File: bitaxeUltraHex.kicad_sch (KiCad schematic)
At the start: 12 parts, among them J1 Conn_01x01, J2 Conn_01x01

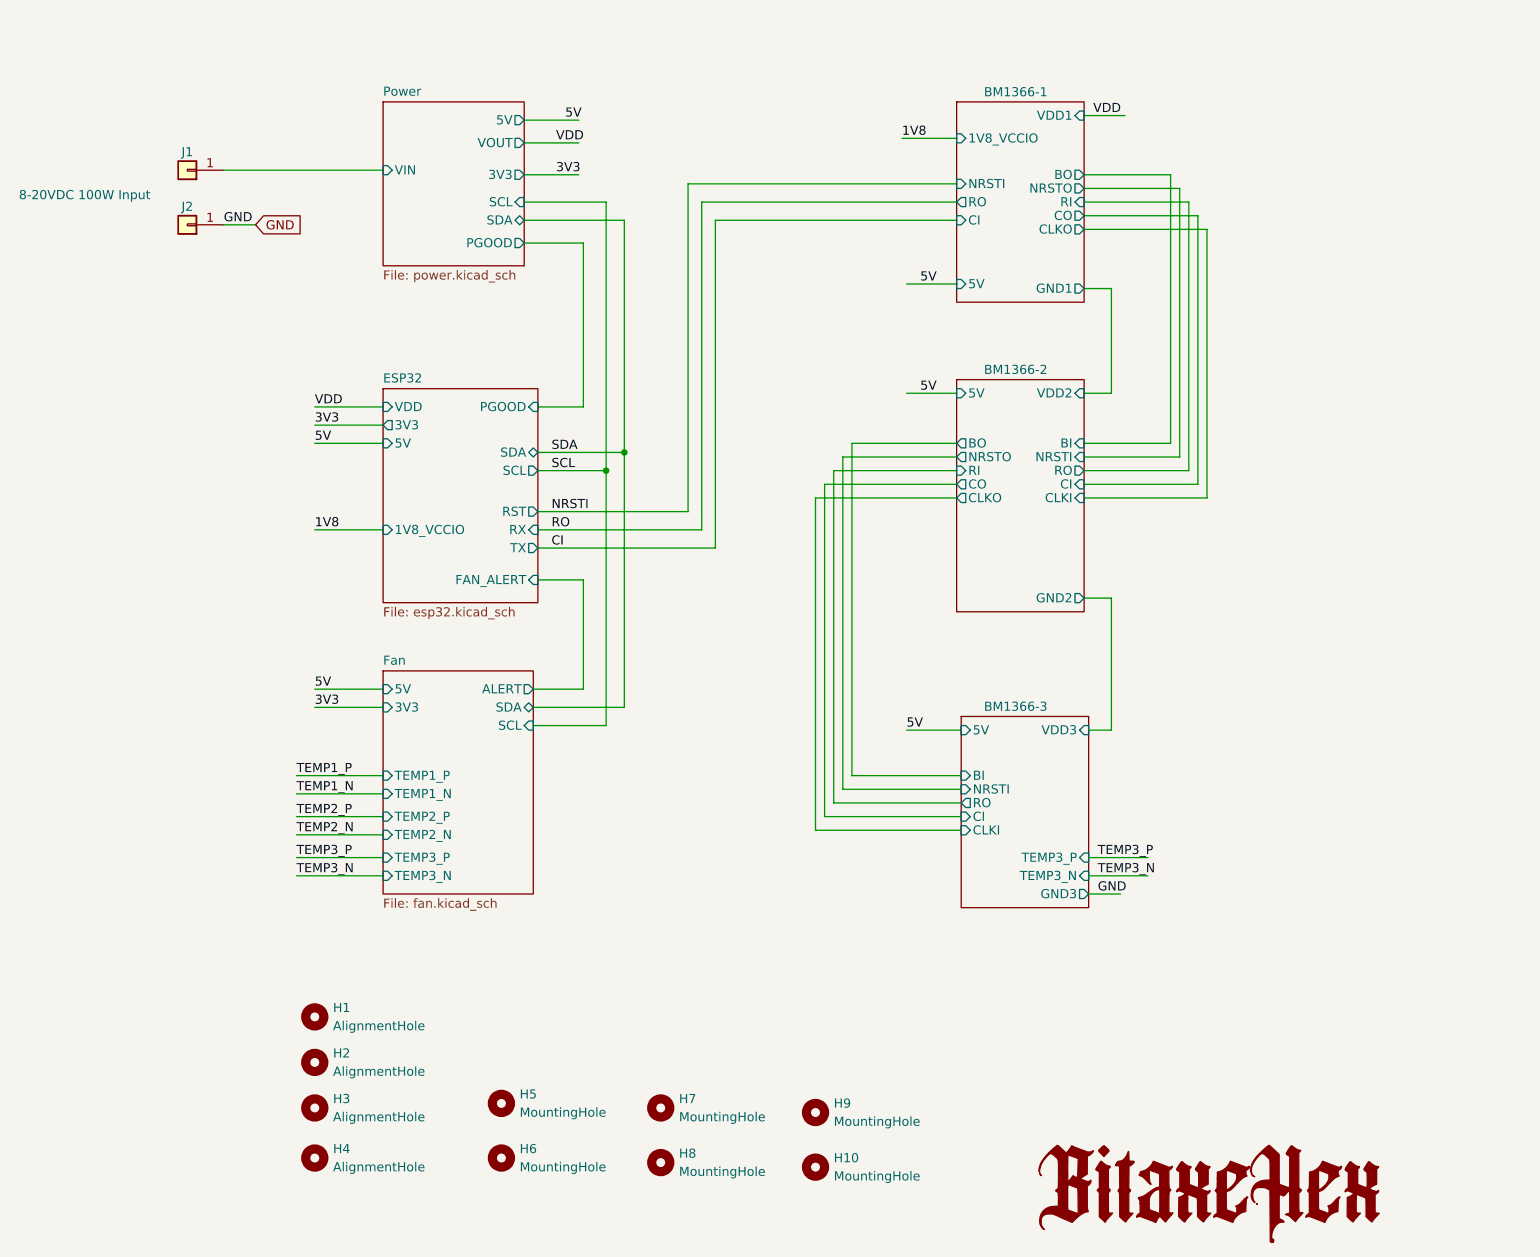
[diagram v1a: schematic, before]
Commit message: cleanup parts and symbol libraries. added TMP1075
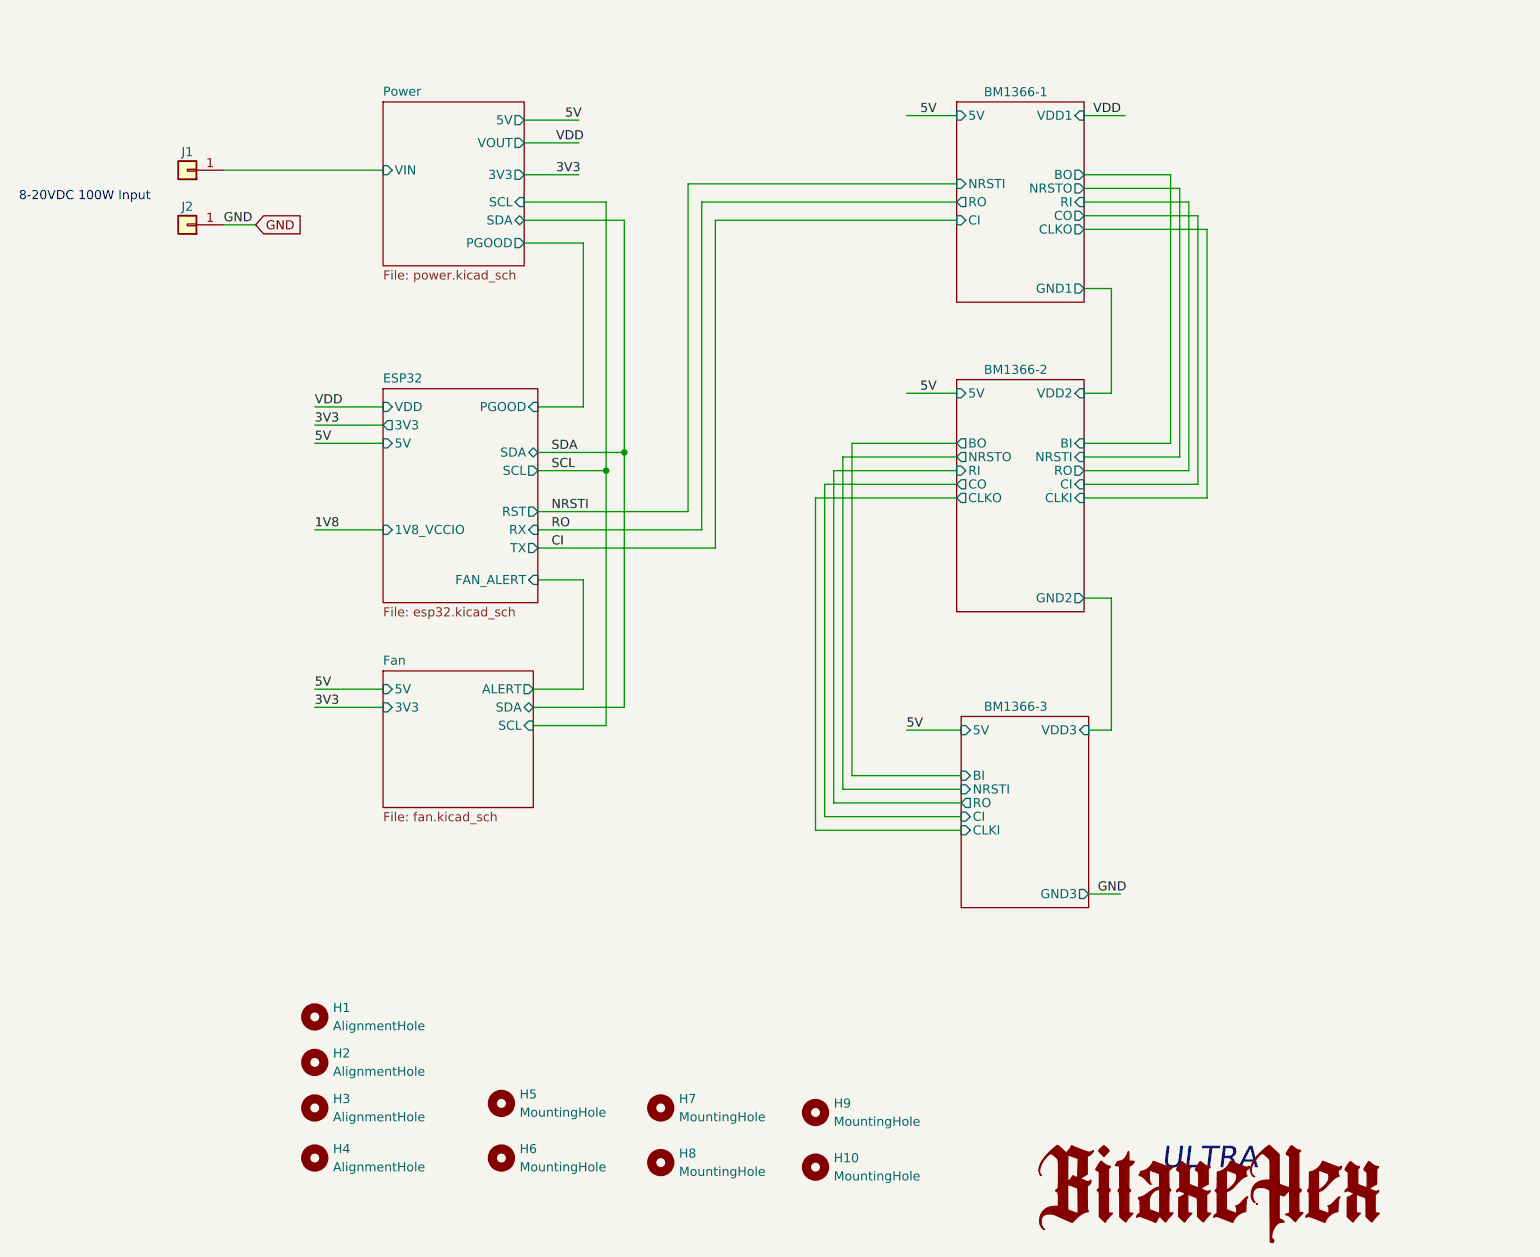
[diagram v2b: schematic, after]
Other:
- sheet BM1366-1 ports: added none; removed 1V8_VCCIO
- sheet BM1366-3 ports: added none; removed TEMP3_N, TEMP3_P
- sheet Fan ports: added none; removed TEMP1_N, TEMP1_P, TEMP2_N, TEMP2_P, TEMP3_N, TEMP3_P
- note added: "ULTRA"
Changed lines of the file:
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@@
-    (stroke (width 0) (type default))
-  )
-  (wire (pts (xy 59.055 128.27) (xy 71.12 128.27))
     (stroke (width 0) (type default))
   )
@@
     (stroke (width 0) (type default))
   )
-  (wire (pts (xy 59.055 136.525) (xy 71.12 136.525))
-    (stroke (width 0) (type default))
-  )
   (wire (pts (xy 144.145 116.205) (xy 151.765 116.205))
     (stroke (width 0) (type default))
@@
     (stroke (width 0) (type default))
   )
-  (wire (pts (xy 59.055 133.985) (xy 71.12 133.985))
-    (stroke (width 0) (type default))
-  )
   (wire (pts (xy 183.515 42.545) (xy 183.515 80.01))
     (stroke (width 0) (type default))
   )
-  (wire (pts (xy 143.51 33.655) (xy 151.13 33.655))
-    (stroke (width 0) (type default))
-  )
-  (wire (pts (xy 144.145 53.975) (xy 151.13 53.975))
+  (wire (pts (xy 144.145 30.48) (xy 151.13 30.48))
     (stroke (width 0) (type default))
   )
@@
     (stroke (width 0) (type default))
   )
-  (wire (pts (xy 59.055 122.555) (xy 71.12 122.555))
-    (stroke (width 0) (type default))
-  )
   (wire (pts (xy 131.445 130.175) (xy 151.765 130.175))
     (stroke (width 0) (type default))
@@
     (stroke (width 0) (type default))
   )
-  (wire (pts (xy 169.545 136.525) (xy 177.8 136.525))
-    (stroke (width 0) (type default))
-  )
   (wire (pts (xy 186.055 83.82) (xy 168.91 83.82))
     (stroke (width 0) (type default))
@@
     (stroke (width 0) (type default))
   )
-  (wire (pts (xy 169.545 133.985) (xy 177.8 133.985))
-    (stroke (width 0) (type default))
-  )
   (wire (pts (xy 135.255 78.105) (xy 135.255 124.46))
     (stroke (width 0) (type default))
@@
     (stroke (width 0) (type default))
   )
-  (wire (pts (xy 59.055 130.81) (xy 71.12 130.81))
-    (stroke (width 0) (type default))
-  )
   (wire (pts (xy 61.595 73.66) (xy 71.12 73.66))
     (stroke (width 0) (type default))
@@
     (stroke (width 0) (type default))
   )
-  (wire (pts (xy 59.055 125.095) (xy 71.12 125.095))
-    (stroke (width 0) (type default))
-  )
   (wire (pts (xy 99.06 110.49) (xy 99.06 95.25))
     (stroke (width 0) (type default))
@@
     (stroke (width 0) (type default))
   )
+  (text "ULTRA" (at 179.705 177.8 0)
+    (effects (font (face "Ayuthaya") (size 3 3) italic) (justify left bottom))
+  )
   (text "8-20VDC 100W Input" (at 20.32 42.545 0)
     (effects (font (size 1.27 1.27)) (justify left bottom))
   )
-  (label "TEMP3_P" (at 59.055 133.985 0) (fields_autoplaced)
-    (effects (font (size 1.27 1.27)) (justify left bottom))
-  )
-  (label "5V" (at 146.05 53.975 0) (fields_autoplaced)
+  (label "5V" (at 146.05 30.48 0) (fields_autoplaced)
     (effects (font (size 1.27 1.27)) (justify left bottom))
   )
@@
     (effects (font (size 1.27 1.27)) (justify left bottom))
   )
-  (label "TEMP3_N" (at 59.055 136.525 0) (fields_autoplaced)
-    (effects (font (size 1.27 1.27)) (justify left bottom))
-  )
   (label "1V8" (at 61.595 88.265 0) (fields_autoplaced)
     (effects (font (size 1.27 1.27)) (justify left bottom))
   )
-  (label "TEMP2_N" (at 59.055 130.81 0) (fields_autoplaced)
-    (effects (font (size 1.27 1.27)) (justify left bottom))
-  )
   (label "5V" (at 96.52 31.115 0) (fields_autoplaced)
     (effects (font (size 1.27 1.27)) (justify left bottom))
@@
     (effects (font (size 1.27 1.27)) (justify left bottom))
   )
-  (label "TEMP2_P" (at 59.055 128.27 0) (fields_autoplaced)
-    (effects (font (size 1.27 1.27)) (justify left bottom))
-  )
   (label "GND" (at 170.815 139.065 0) (fields_autoplaced)
     (effects (font (size 1.27 1.27)) (justify left bottom))
@@
     (effects (font (size 1.27 1.27)) (justify left bottom))
   )
-  (label "TEMP3_P" (at 170.815 133.985 0) (fields_autoplaced)
-    (effects (font (size 1.27 1.27)) (justify left bottom))
-  )
   (label "CI" (at 94.615 90.805 0) (fields_autoplaced)
     (effects (font (size 1.27 1.27)) (justify left bottom))
@@
     (effects (font (size 1.27 1.27)) (justify left bottom))
   )
-  (label "1V8" (at 143.51 33.655 0) (fields_autoplaced)
-    (effects (font (size 1.27 1.27)) (justify left bottom))
-  )
   (label "3V3" (at 61.595 113.03 0) (fields_autoplaced)
     (effects (font (size 1.27 1.27)) (justify left bottom))
@@
     (effects (font (size 1.27 1.27)) (justify left bottom))
   )
-  (label "TEMP1_N" (at 59.055 125.095 0) (fields_autoplaced)
-    (effects (font (size 1.27 1.27)) (justify left bottom))
-  )
   (label "RO" (at 94.615 88.265 0) (fields_autoplaced)
     (effects (font (size 1.27 1.27)) (justify left bottom))
   )
-  (label "TEMP1_P" (at 59.055 122.555 0) (fields_autoplaced)
-    (effects (font (size 1.27 1.27)) (justify left bottom))
-  )
   (label "VDD" (at 95.25 34.29 0) (fields_autoplaced)
-    (effects (font (size 1.27 1.27)) (justify left bottom))
-  )
-  (label "TEMP3_N" (at 170.815 136.525 0) (fields_autoplaced)
     (effects (font (size 1.27 1.27)) (justify left bottom))
   )
@@
       (effects (font (size 1.27 1.27)) (justify left))
     )
-    (pin "5V" input (at 151.13 53.975 180)
+    (pin "5V" input (at 151.13 30.48 180)
       (effects (font (size 1.27 1.27)) (justify left))
     )
@@
     (pin "GND1" output (at 168.91 54.61 0)
       (effects (font (size 1.27 1.27)) (justify right))
-    )
-    (pin "1V8_VCCIO" input (at 151.13 33.655 180)
-      (effects (font (size 1.27 1.27)) (justify left))
     )
     (instances
@@
     )
   )
-  (sheet (at 71.12 107.95) (size 20.955 31.115) (fields_autoplaced)
+  (sheet (at 71.12 107.95) (size 20.955 19.05) (fields_autoplaced)
     (stroke (width 0.1524) (type solid))
     (fill (color 255 255 194 1.0000))
@@
       (effects (font (size 1.27 1.27)) (justify left bottom))
     )
-    (property "Sheetfile" "fan.kicad_sch" (at 71.12 139.6496 0)
+    (property "Sheetfile" "fan.kicad_sch" (at 71.12 127.5846 0)
       (effects (font (size 1.27 1.27)) (justify left top))
     )
@@
     (pin "ALERT" output (at 92.075 110.49 0)
       (effects (font (size 1.27 1.27)) (justify right))
-    )
-    (pin "TEMP2_P" input (at 71.12 128.27 180)
-      (effects (font (size 1.27 1.27)) (justify left))
-    )
-    (pin "TEMP2_N" input (at 71.12 130.81 180)
-      (effects (font (size 1.27 1.27)) (justify left))
-    )
-    (pin "TEMP1_P" input (at 71.12 122.555 180)
-      (effects (font (size 1.27 1.27)) (justify left))
-    )
-    (pin "TEMP1_N" input (at 71.12 125.095 180)
-      (effects (font (size 1.27 1.27)) (justify left))
-    )
-    (pin "TEMP3_P" input (at 71.12 133.985 180)
-      (effects (font (size 1.27 1.27)) (justify left))
-    )
-    (pin "TEMP3_N" input (at 71.12 136.525 180)
-      (effects (font (size 1.27 1.27)) (justify left))
     )
     (instances
@@
       (effects (font (size 1.27 1.27)) (justify right))
     )
-    (pin "TEMP3_P" input (at 169.545 133.985 0)
-      (effects (font (size 1.27 1.27)) (justify right))
-    )
-    (pin "TEMP3_N" input (at 169.545 136.525 0)
-      (effects (font (size 1.27 1.27)) (justify right))
-    )

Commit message: moved all custom symbols and footprints to the bitaxe library
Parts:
- J1, J2: footprint TPS40305_supply:63862-1 -> bitaxe:63862-1
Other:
- title: bitaxeHex -> bitaxeUltraHex
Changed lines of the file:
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@@
   (paper "A")
   (title_block
-    (title "bitaxeHex")
+    (title "bitaxeUltraHex")
     (date "2023-06-11")
     (rev "1")
@@
       (effects (font (size 1.27 1.27)) hide)
     )
-    (property "Footprint" "TPS40305_supply:63862-1" (at 43.815 38.1 0)
+    (property "Footprint" "bitaxe:63862-1" (at 43.815 38.1 0)
       (effects (font (size 1.27 1.27)) hide)
     )
@@
     )
   )
-  (symbol (lib_id "Bitaxe:LOGO") (at 186.055 180.975 0) (unit 1)
+  (symbol (lib_id "bitaxe:Bitaxe_Hex_Logo") (at 186.055 180.975 0) (unit 1)
     (in_bom yes) (on_board yes) (dnp no) (fields_autoplaced)
     (property "Reference" "#G1" (at 186.055 174.0216 0)
@@
       (effects (font (size 1.27 1.27)) hide)
     )
-    (property "Footprint" "TPS40305_supply:63862-1" (at 43.815 45.72 0)
-      (effects (font (size 1.27 1.27)) hide)
-    )
+    (property "Footprint" "bitaxe:63862-1" (at 43.815 45.72 0)
+      (effects (font (size 1.27 1.27)) hide)
+    )
